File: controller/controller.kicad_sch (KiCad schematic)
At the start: 0 parts

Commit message: relay h bridge
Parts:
- added D1, D?: 1N4007, Diode_THT:D_DO-41_SOD81_P10.16mm_Horizontal, symbol Diode:1N4007
- added D? (x3): LED, symbol Device:LED
- added F1: Fuse, symbol Device:Fuse
- added J1: Conn_01x02_Pin, symbol Connector:Conn_01x02_Pin
- added M1: Motor_DC, symbol Motor:Motor_DC
- added R1, R2, R3: 470, symbol Device:R
- added SW1: SW_DPDT_x2, symbol Switch:SW_DPDT_x2
- added SW2, SW3: SW_SPST, symbol Switch:SW_SPST
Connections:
- new net: F1.1, J1.1 (Pin_1)
- new net: F1.2, J1.2 (Pin_2), R2.1
- new net: D?.1 (K), SW2.1 (A), SW3.1 (A)
- new net: R1.1, SW3.2 (B)
- new net: D?.1 (K), SW1.5 (B)
- new net: D?.2 (A), R3.2
- new net: D?.1 (K), SW1.2 (B)
- new net: D?.2 (A), R1.2
- new net: R3.1, SW2.2 (B)
- new net: M1.2 (-), SW1.3 (C), SW1.4 (A)
- new net: M1.1 (+), SW1.1 (A), SW1.6 (C)
- new net: D?.2 (A), R2.2

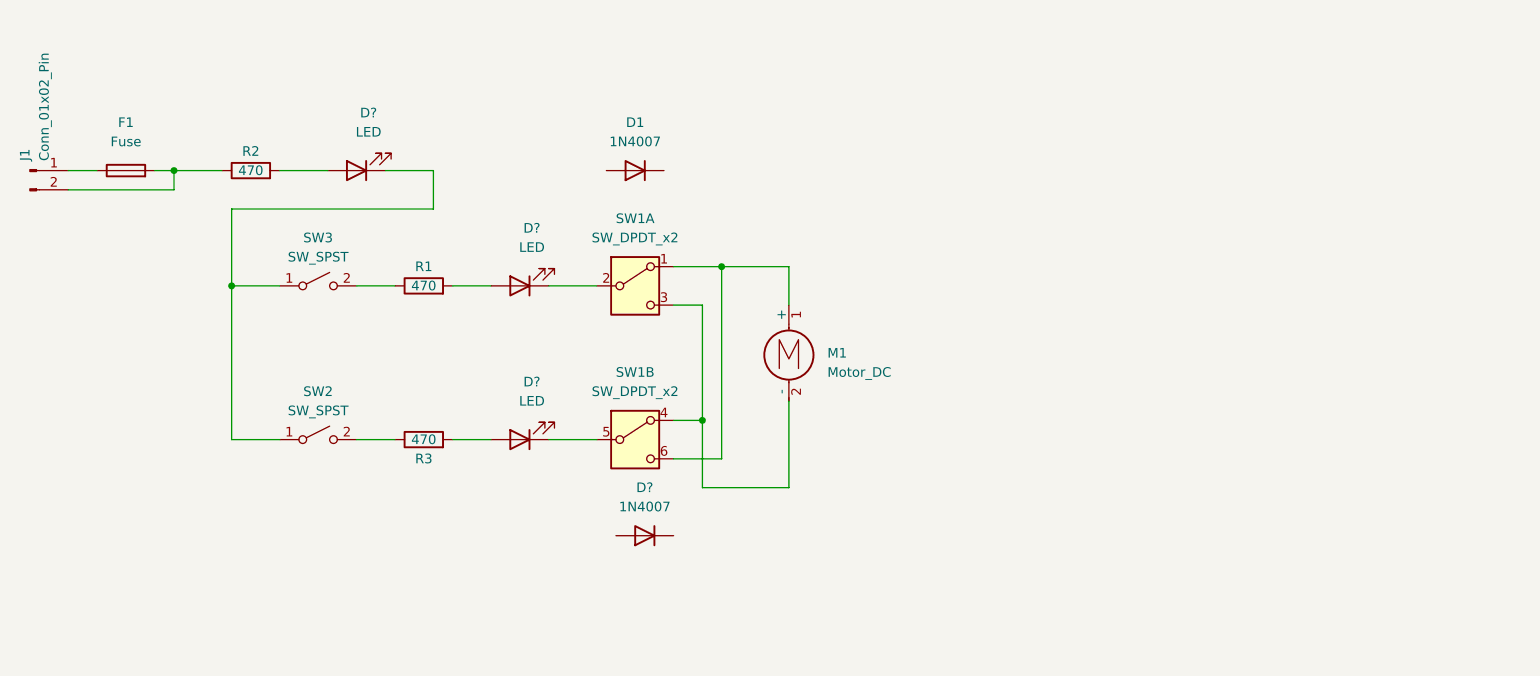
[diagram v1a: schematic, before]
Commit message: relay sw motor
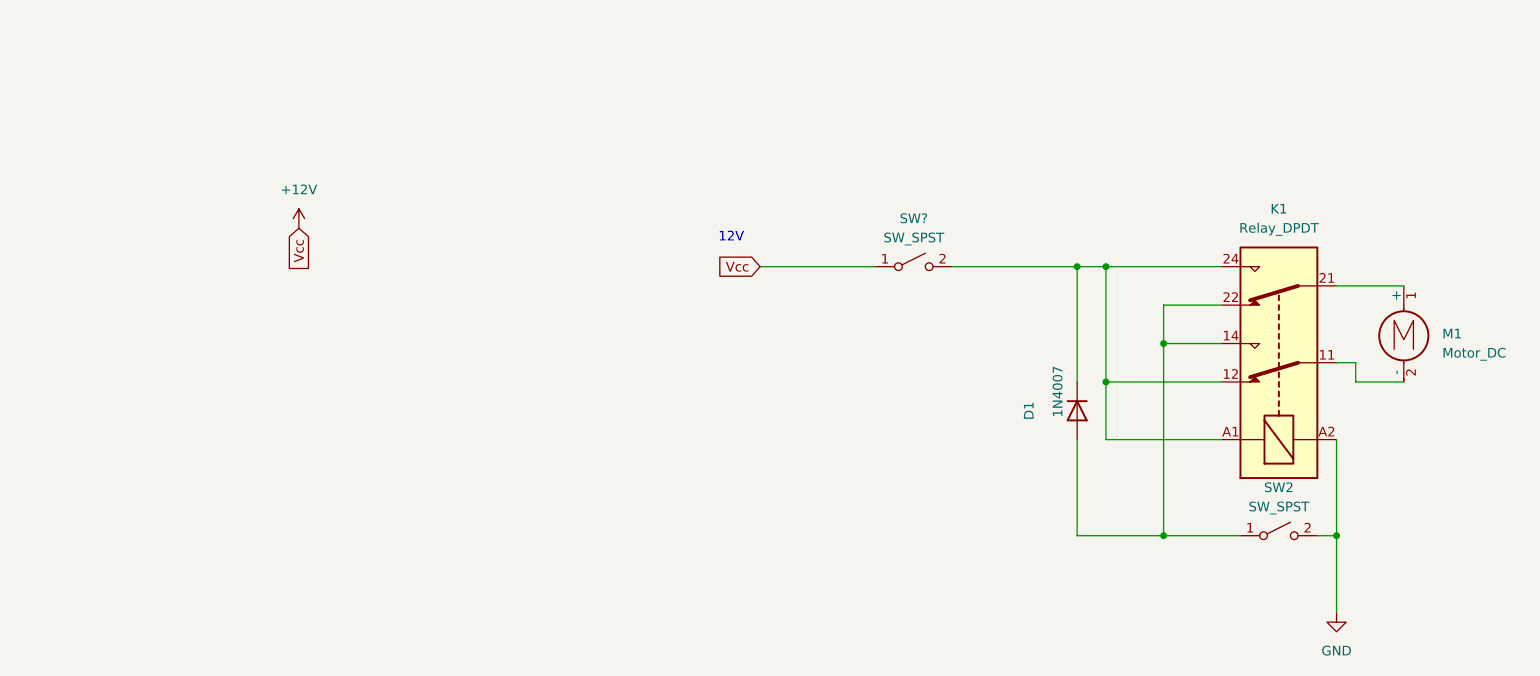
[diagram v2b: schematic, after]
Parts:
- removed D? (x3): LED, symbol Device:LED
- removed D?: 1N4007, Diode_THT:D_DO-41_SOD81_P10.16mm_Horizontal, symbol Diode:1N4007
- removed F1: Fuse, symbol Device:Fuse
- removed J1: Conn_01x02_Pin, symbol Connector:Conn_01x02_Pin
- removed R1, R2, R3: 470, symbol Device:R
- removed SW1: SW_DPDT_x2, symbol Switch:SW_DPDT_x2
- removed SW3: SW_SPST, symbol Switch:SW_SPST
- added K1: Relay_DPDT, symbol Relay:Relay_DPDT
- added SW?: SW_SPST, symbol Switch:SW_SPST
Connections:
- net at D1.1 (K): now also K1.12, K1.24, K1.A1, SW?.2 (B)
- net at D1.2 (A): now also SW2.1 (A), K1.14, K1.22
- net GND: now reaches SW2.2 (B)
- net GND: now also K1.A2
- net at M1.2 (-): now also K1.11
- net at M1.1 (+): now also K1.21
- new net +12V: SW?.1 (A)
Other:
- note added: "12V"
- moved on the sheet: D1, M1

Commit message: vcc output vin npn collector amp
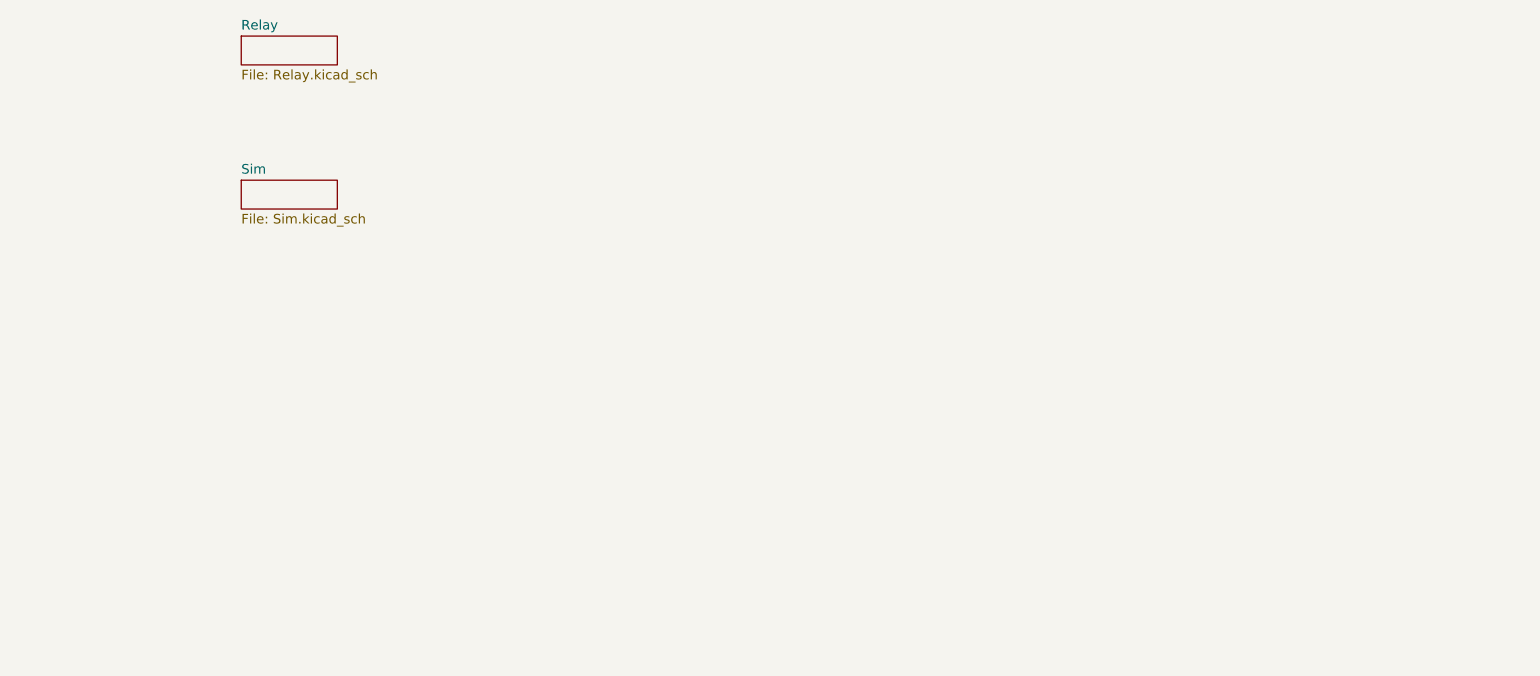
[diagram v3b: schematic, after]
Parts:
- removed D1: 1N4007, Diode_THT:D_DO-41_SOD81_P10.16mm_Horizontal, symbol Diode:1N4007
- removed K1: Relay_DPDT, symbol Relay:Relay_DPDT
- removed M1: Motor_DC, symbol Motor:Motor_DC
- removed SW2, SW?: SW_SPST, symbol Switch:SW_SPST
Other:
- added sheet Relay (Relay.kicad_sch)
- added sheet Sim (Sim.kicad_sch)
- note removed: "12V"
